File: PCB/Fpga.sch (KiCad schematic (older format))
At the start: 7 parts, among them U2 10CL016YE144C8G

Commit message: Route more signals
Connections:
- net DFI_1: now also U2.136 (PIN_136); no longer U2.59 (PIN_59)
- net DFI_2: now also U2.137 (PIN_137); no longer U2.60 (PIN_60)
- net Dome_LED: now also U2.83 (PIN_83); no longer U2.58 (PIN_58)
- net Extension_1: now also U2.142 (PIN_142); no longer U2.141 (PIN_141)
- net Extension_2: now also U2.144 (PIN_144); no longer U2.142 (PIN_142)
- net Extension_4: now also U2.141 (PIN_141); no longer U2.144 (PIN_144)
- net Hall_sensor_L: now also U2.46 (PIN_46); no longer U2.136 (PIN_136)
- net Hall_sensor_R: now also U2.44 (PIN_44); no longer U2.137 (PIN_137)
- net Light_sensor_INT: now also U2.112 (PIN_112); no longer U2.113 (PIN_113)
- net Light_sensor_SCL: now also U2.113 (PIN_113); no longer U2.112 (PIN_112)
- net Motor_PWM_1: now also U2.59 (PIN_59); no longer U2.44 (PIN_44)
- net Motor_PWM_2: now also U2.60 (PIN_60); no longer U2.46 (PIN_46)
- net Weight: now also U2.67 (PIN_67); no longer U2.68 (PIN_68)
- net Weight_FSR: now also U2.66 (PIN_66); no longer U2.67 (PIN_67)
- net Weight_ref: now also U2.68 (PIN_68); no longer U2.66 (PIN_66)
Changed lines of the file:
@@
 Text HLabel 9000 4600 2    50   Output ~ 0
 Power_LED_R
-Text HLabel 4500 3000 2    50   Output ~ 0
+Text HLabel 4500 4800 2    50   Output ~ 0
 Motor_PWM_2
-Text HLabel 4500 2900 2    50   Output ~ 0
+Text HLabel 4500 4700 2    50   Output ~ 0
 Motor_PWM_1
-Text HLabel 4500 4600 2    50   Output ~ 0
+Text HLabel 9000 1400 2    50   Output ~ 0
 Dome_LED
 Text HLabel 9000 2600 2    50   BiDi ~ 0
 Light_sensor_SDA
-Text HLabel 9000 2700 2    50   Output ~ 0
+Text HLabel 9000 2800 2    50   Output ~ 0
 Light_sensor_SCL
-Text HLabel 9000 2800 2    50   Input ~ 0
+Text HLabel 9000 2700 2    50   Input ~ 0
 Light_sensor_INT
 $Sheet
@@
 	8650 4800 9000 4800
 Wire Wire Line
-	4150 4600 4500 4600
-Text HLabel 9000 5100 2    50   BiDi ~ 0
+	8650 1400 9000 1400
+Text HLabel 9000 5200 2    50   BiDi ~ 0
 Extension_1
 Wire Wire Line
@@
 Wire Wire Line
 	8650 5300 9000 5300
-Text HLabel 9000 5200 2    50   BiDi ~ 0
+Text HLabel 9000 5400 2    50   BiDi ~ 0
 Extension_2
 Text HLabel 9000 5300 2    50   BiDi ~ 0
@@
 Wire Wire Line
 	8650 5400 9000 5400
-Text HLabel 9000 5400 2    50   BiDi ~ 0
+Text HLabel 9000 5100 2    50   BiDi ~ 0
 Extension_4
 Wire Wire Line
@@
 Wire Wire Line
 	6250 5400 6750 5400
-Text HLabel 4500 4700 2    50   BiDi ~ 0
-DFI_1
 Wire Wire Line
 	4150 4700 4500 4700
 Wire Wire Line
 	4500 4800 4150 4800
-Text HLabel 4500 4800 2    50   BiDi ~ 0
-DFI_2
+Text HLabel 4500 5200 2    50   Output ~ 0
+Weight_ref
 Text HLabel 4500 5000 2    50   Output ~ 0
-Weight_ref
-Text HLabel 4500 5100 2    50   Output ~ 0
 Weight_FSR
-Text HLabel 4500 5200 2    50   3State ~ 0
+Text HLabel 4500 5100 2    50   3State ~ 0
 Weight
 Wire Wire Line
@@
 Wire Wire Line
 	4500 5200 4150 5200
-Text HLabel 9000 4900 2    50   Input ~ 0
+Text HLabel 4500 3000 2    50   Input ~ 0
 Hall_sensor_L
 Wire Wire Line
 	8650 4900 9000 4900
-Text HLabel 9000 5000 2    50   Input ~ 0
+Text HLabel 4500 2900 2    50   Input ~ 0
 Hall_sensor_R
 Wire Wire Line
@@
 NoConn ~ 8650 3000
 NoConn ~ 8650 2900
-NoConn ~ 8650 1400
 NoConn ~ 4150 4900
 Text HLabel 2000 6600 0    50   Output ~ 0
@@
 Wire Wire Line
 	2000 6900 2500 6900
+Text HLabel 9000 5000 2    50   BiDi ~ 0
+DFI_2
+Text HLabel 9000 4900 2    50   BiDi ~ 0
+DFI_1
+NoConn ~ 4150 4600
 $EndSCHEMATC

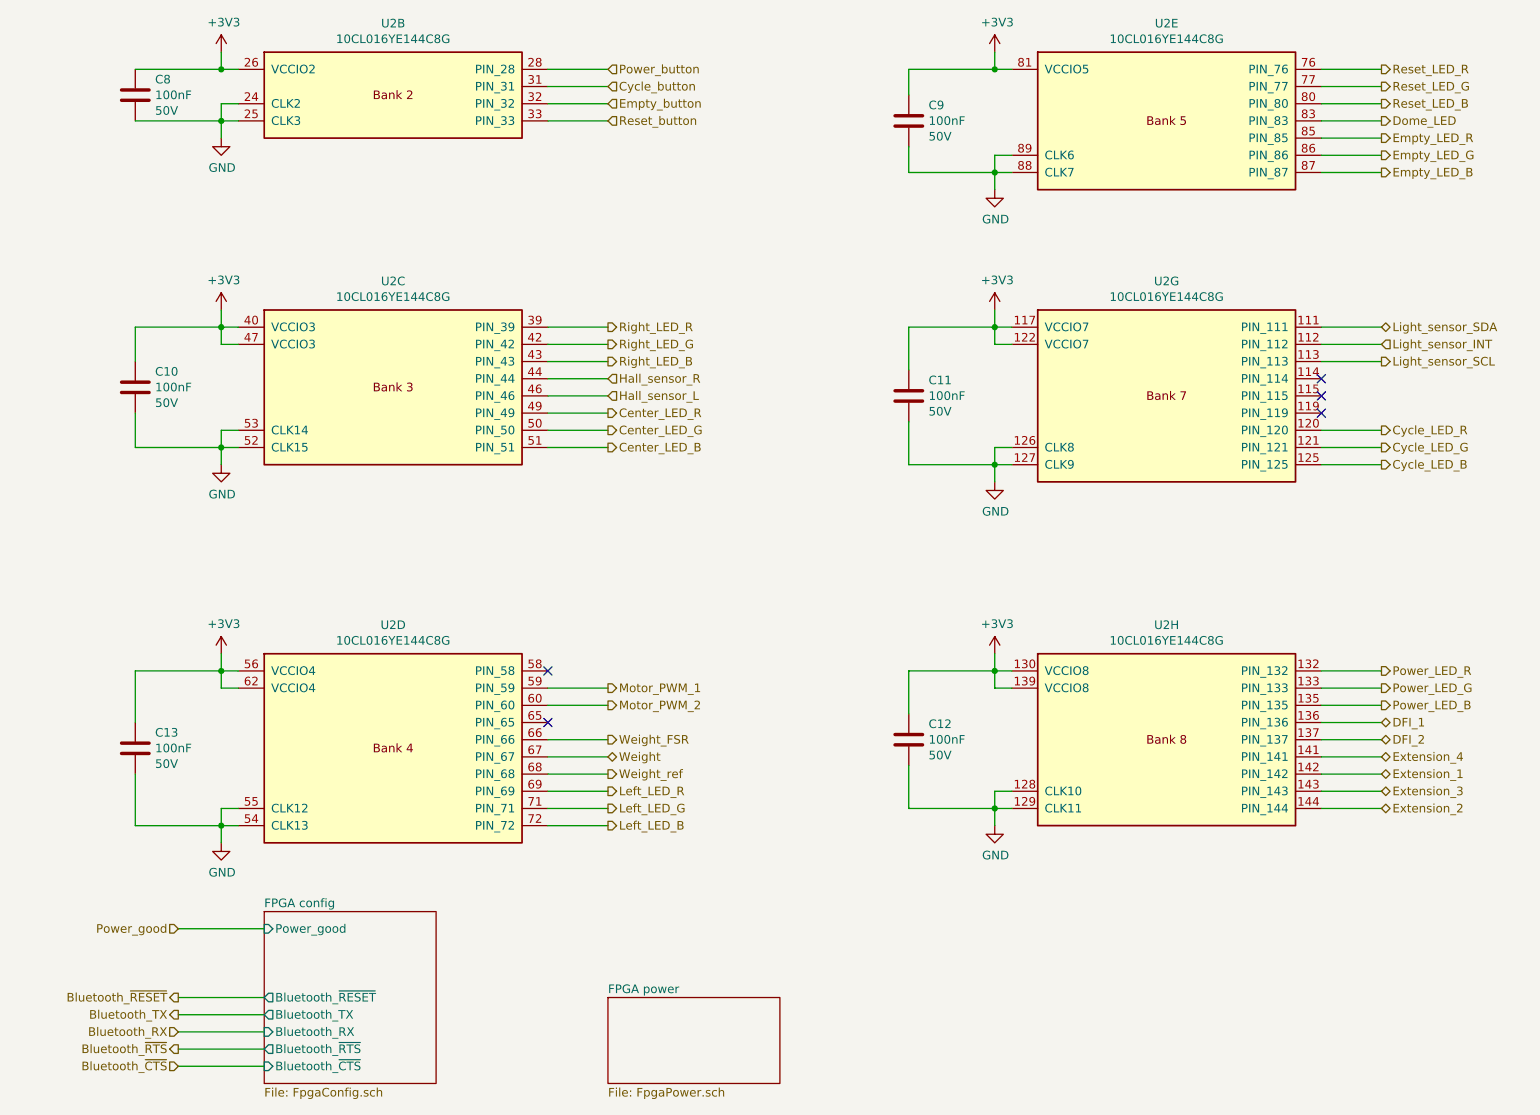
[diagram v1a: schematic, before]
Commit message: Complete routing all signals
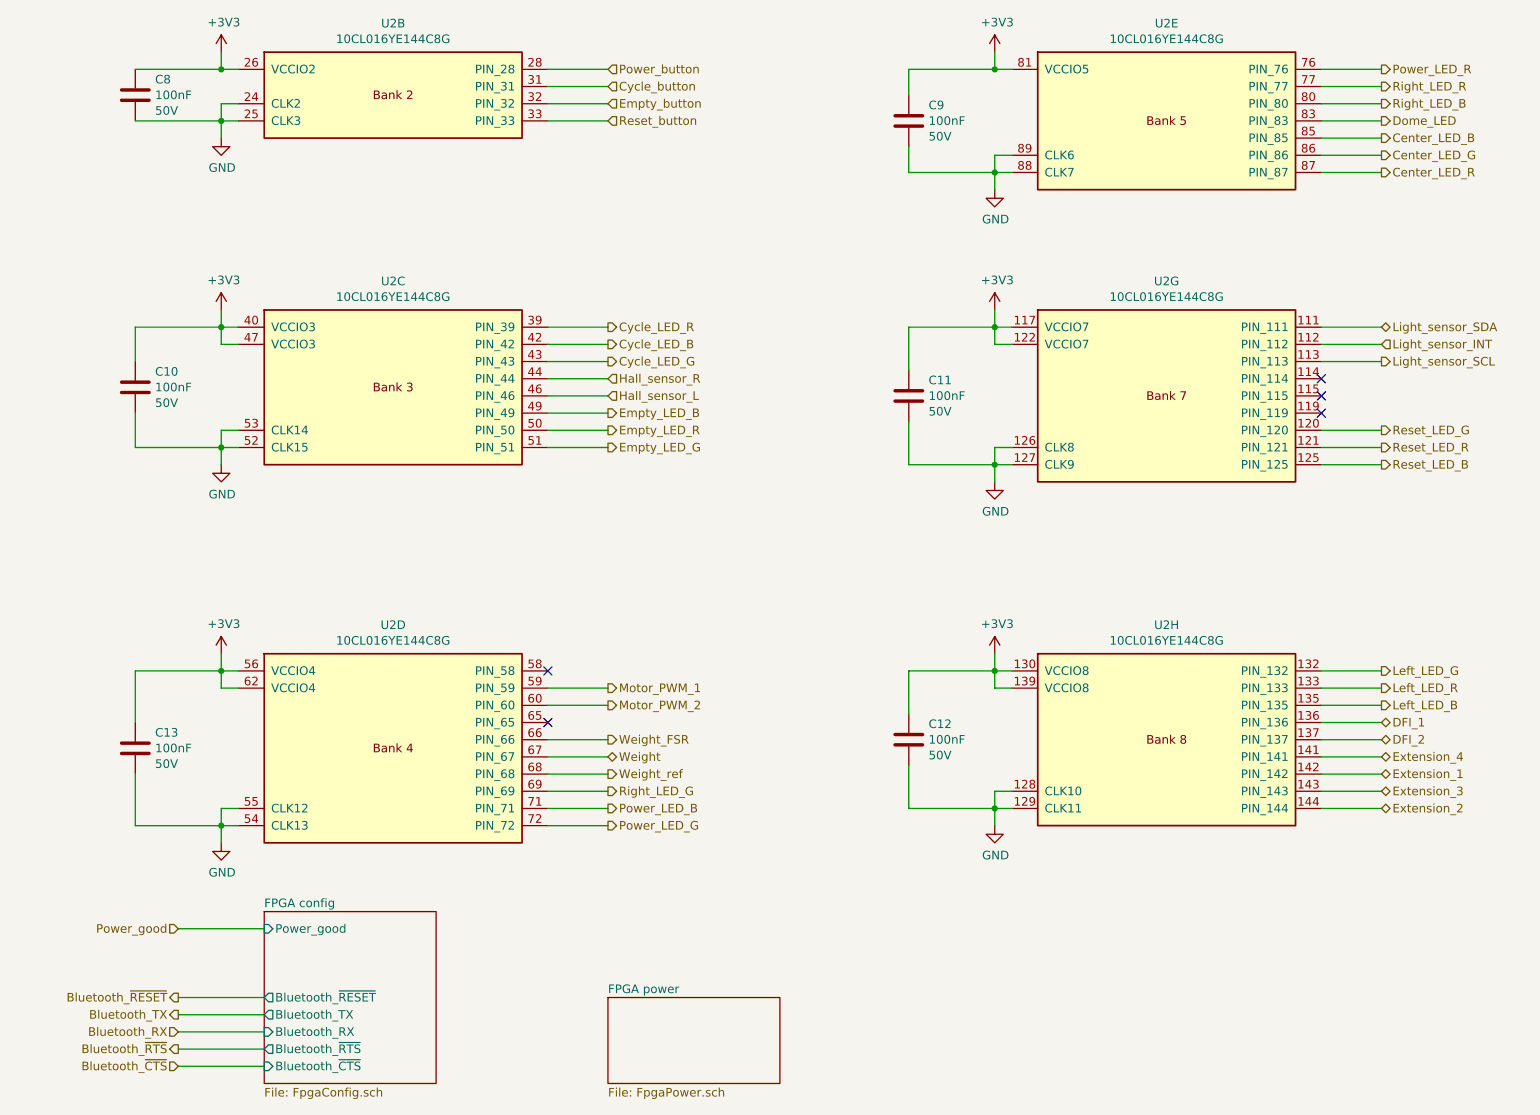
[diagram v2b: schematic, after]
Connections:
- net Center_LED_B: now also U2.85 (PIN_85); no longer U2.51 (PIN_51)
- net Center_LED_G: now also U2.86 (PIN_86); no longer U2.50 (PIN_50)
- net Center_LED_R: now also U2.87 (PIN_87); no longer U2.49 (PIN_49)
- net Cycle_LED_B: now also U2.42 (PIN_42); no longer U2.125 (PIN_125)
- net Cycle_LED_G: now also U2.43 (PIN_43); no longer U2.121 (PIN_121)
- net Cycle_LED_R: now also U2.39 (PIN_39); no longer U2.120 (PIN_120)
- net Empty_LED_B: now also U2.49 (PIN_49); no longer U2.87 (PIN_87)
- net Empty_LED_G: now also U2.51 (PIN_51); no longer U2.86 (PIN_86)
- net Empty_LED_R: now also U2.50 (PIN_50); no longer U2.85 (PIN_85)
- net Left_LED_B: now also U2.135 (PIN_135); no longer U2.72 (PIN_72)
- net Left_LED_G: now also U2.132 (PIN_132); no longer U2.71 (PIN_71)
- net Left_LED_R: now also U2.133 (PIN_133); no longer U2.69 (PIN_69)
- net Power_LED_B: now also U2.71 (PIN_71); no longer U2.135 (PIN_135)
- net Power_LED_G: now also U2.72 (PIN_72); no longer U2.133 (PIN_133)
- net Power_LED_R: now also U2.76 (PIN_76); no longer U2.132 (PIN_132)
- net Reset_LED_B: now also U2.125 (PIN_125); no longer U2.80 (PIN_80)
- net Reset_LED_G: now also U2.120 (PIN_120); no longer U2.77 (PIN_77)
- net Reset_LED_R: now also U2.121 (PIN_121); no longer U2.76 (PIN_76)
- net Right_LED_B: now also U2.80 (PIN_80); no longer U2.43 (PIN_43)
- net Right_LED_G: now also U2.69 (PIN_69); no longer U2.42 (PIN_42)
- net Right_LED_R: now also U2.77 (PIN_77); no longer U2.39 (PIN_39)
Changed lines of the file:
@@
 Text HLabel 4500 1400 2    50   Input ~ 0
 Reset_button
+Text HLabel 4500 2600 2    50   Output ~ 0
+Cycle_LED_R
+Text HLabel 4500 2800 2    50   Output ~ 0
+Cycle_LED_G
+Text HLabel 4500 2700 2    50   Output ~ 0
+Cycle_LED_B
+Text HLabel 4500 3200 2    50   Output ~ 0
+Empty_LED_R
+Text HLabel 4500 3300 2    50   Output ~ 0
+Empty_LED_G
+Text HLabel 4500 3100 2    50   Output ~ 0
+Empty_LED_B
 Text HLabel 9000 3200 2    50   Output ~ 0
-Cycle_LED_R
-Text HLabel 9000 3300 2    50   Output ~ 0
-Cycle_LED_G
+Reset_LED_G
 Text HLabel 9000 3400 2    50   Output ~ 0
-Cycle_LED_B
+Reset_LED_B
+Text HLabel 9000 4700 2    50   Output ~ 0
+Left_LED_R
+Text HLabel 9000 4600 2    50   Output ~ 0
+Left_LED_G
+Text HLabel 9000 4800 2    50   Output ~ 0
+Left_LED_B
+Text HLabel 9000 1700 2    50   Output ~ 0
+Center_LED_R
+Text HLabel 9000 1600 2    50   Output ~ 0
+Center_LED_G
 Text HLabel 9000 1500 2    50   Output ~ 0
-Empty_LED_R
-Text HLabel 9000 1600 2    50   Output ~ 0
-Empty_LED_G
-Text HLabel 9000 1700 2    50   Output ~ 0
-Empty_LED_B
-Text HLabel 9000 1100 2    50   Output ~ 0
-Reset_LED_R
-Text HLabel 9000 1200 2    50   Output ~ 0
-Reset_LED_G
+Center_LED_B
+Text HLabel 4500 5300 2    50   Output ~ 0
+Right_LED_G
 Text HLabel 9000 1300 2    50   Output ~ 0
-Reset_LED_B
-Text HLabel 4500 5300 2    50   Output ~ 0
-Left_LED_R
-Text HLabel 4500 5400 2    50   Output ~ 0
-Left_LED_G
-Text HLabel 4500 5500 2    50   Output ~ 0
-Left_LED_B
-Text HLabel 4500 3100 2    50   Output ~ 0
-Center_LED_R
-Text HLabel 4500 3200 2    50   Output ~ 0
-Center_LED_G
-Text HLabel 4500 3300 2    50   Output ~ 0
-Center_LED_B
-Text HLabel 4500 2600 2    50   Output ~ 0
-Right_LED_R
-Text HLabel 4500 2700 2    50   Output ~ 0
-Right_LED_G
-Text HLabel 4500 2800 2    50   Output ~ 0
 Right_LED_B
 Text HLabel 4500 1100 2    50   Input ~ 0
@@
 Text HLabel 2000 6100 0    50   Input ~ 0
 Power_good
-Text HLabel 9000 4800 2    50   Output ~ 0
+Text HLabel 4500 5400 2    50   Output ~ 0
 Power_LED_B
-Text HLabel 9000 4700 2    50   Output ~ 0
+Text HLabel 4500 5500 2    50   Output ~ 0
 Power_LED_G
-Text HLabel 9000 4600 2    50   Output ~ 0
-Power_LED_R
 Text HLabel 4500 4800 2    50   Output ~ 0
 Motor_PWM_2
@@
 DFI_1
 NoConn ~ 4150 4600
+Text HLabel 9000 1100 2    50   Output ~ 0
+Power_LED_R
+Text HLabel 9000 3300 2    50   Output ~ 0
+Reset_LED_R
+Text HLabel 9000 1200 2    50   Output ~ 0
+Right_LED_R
 $EndSCHEMATC
